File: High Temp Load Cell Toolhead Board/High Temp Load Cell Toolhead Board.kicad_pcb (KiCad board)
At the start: 6 copper layers, 60 x 60 mm, 123 parts, among them J1 Conn_01x03, J11 Conn_01x03, J12 Conn_01x03, J13 PinHeader_2x4_P2.54mm, J2 Conn_02x08, J6 Conn_01x04, J7 Conn_01x02, J8 Conn_01x04, J9 Conn_01x02, P1 USB_C_Plug_USB2.0, Q1 CSD17581Q3A, Q2 CSD17581Q3A, SW1 SW_SPST, U1 SN74LVC2G17DSFR, U2 STM32F103CBU6TR, U3 SN74LVC2G17DSFR, U5 ADS1220, Y1 Crystal

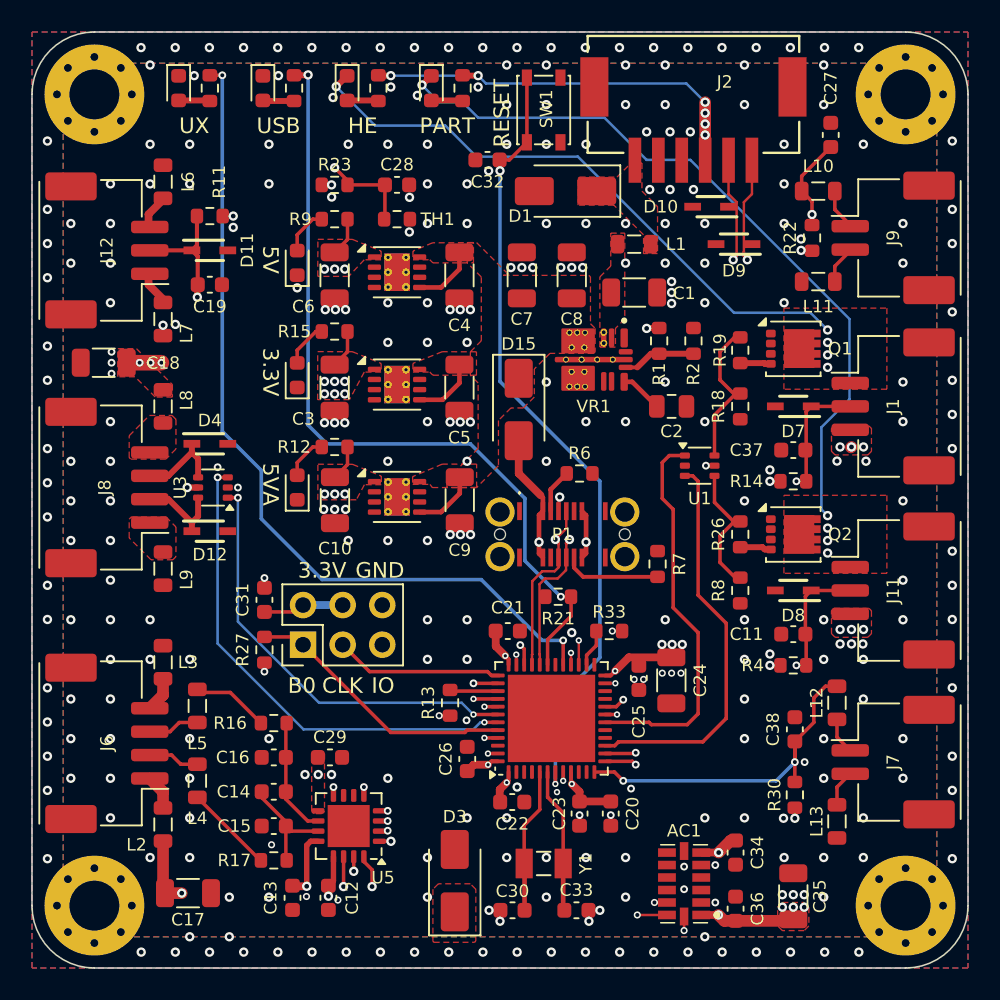
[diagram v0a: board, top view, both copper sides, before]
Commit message: Update 5V Power input
* Changed 5V USB power to rout in via the main 24V power input. This assumes the buck converter can operate in dropout mode and pass the 5V supply to the LDOs. This avoids potential issues with backfeeding the buck converter.
* Added a klipper pins file to give meaningful names to pins
* Added do-not-populate bypass resistors for fans to test tachometer behavior
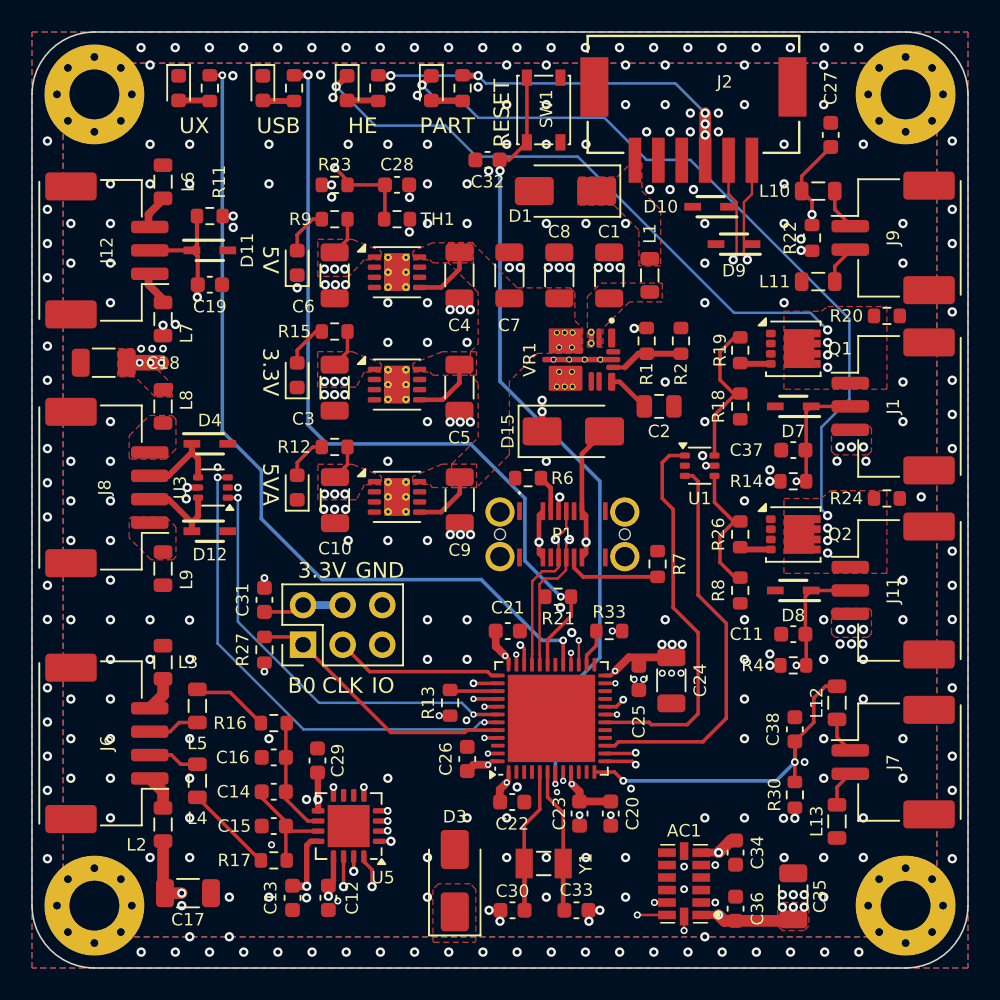
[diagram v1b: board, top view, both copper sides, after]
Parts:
- added R20: R20kΩ, Resistor_SMD:R_0603_1608Metric, F.Cu at (54.8, 18.2)
- added R24: R20kΩ, Resistor_SMD:R_0603_1608Metric, F.Cu at (54.8, 29.9)
- moved D15 3.77 mm to (34.7, 25.6), turned to 0 degrees
- moved R6 3.31 mm to (31.8, 28.6), turned to 180 degrees
- moved L1 2.24 mm to (39.6, 15.6), turned to -90 degrees
- moved C1 1.94 mm to (37.0, 15.6), turned to 90 degrees
- moved C29 0.82 mm to (18.3, 46.7), turned to 90 degrees
- moved C8 0.80 mm to (33.8, 15.6)
- moved R1 0.80 mm to (39.4, 19.8)
- moved C2 0.80 mm to (40.2, 24.0)
- moved C7 0.80 mm to (30.6, 15.6)
- moved R2 0.80 mm to (41.6, 19.8)
- moved VR1 0.80 mm to (35.2, 21.0)
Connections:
- D15 pad 1: +5V5 -> +24V
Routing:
- net +24V: track 0.00 -> 9.56 mm, vias 0 -> 1
- net +5VA: track 58.8 -> 62.8 mm
- net /+FANV_INPUT: track 70.1 -> 69.3 mm, vias 12 -> 11
- net /+5V_USB: track 15.8 -> 16.4 mm
- net +3V3: vias 27 -> 24

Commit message: Add Thermal Reliefs
* Enable thermal relief on GND and 3.3V
* Re-work 5.5V zone to support thermal relief
* Move vias off of silkscreen
* Fix vias that are close to pads
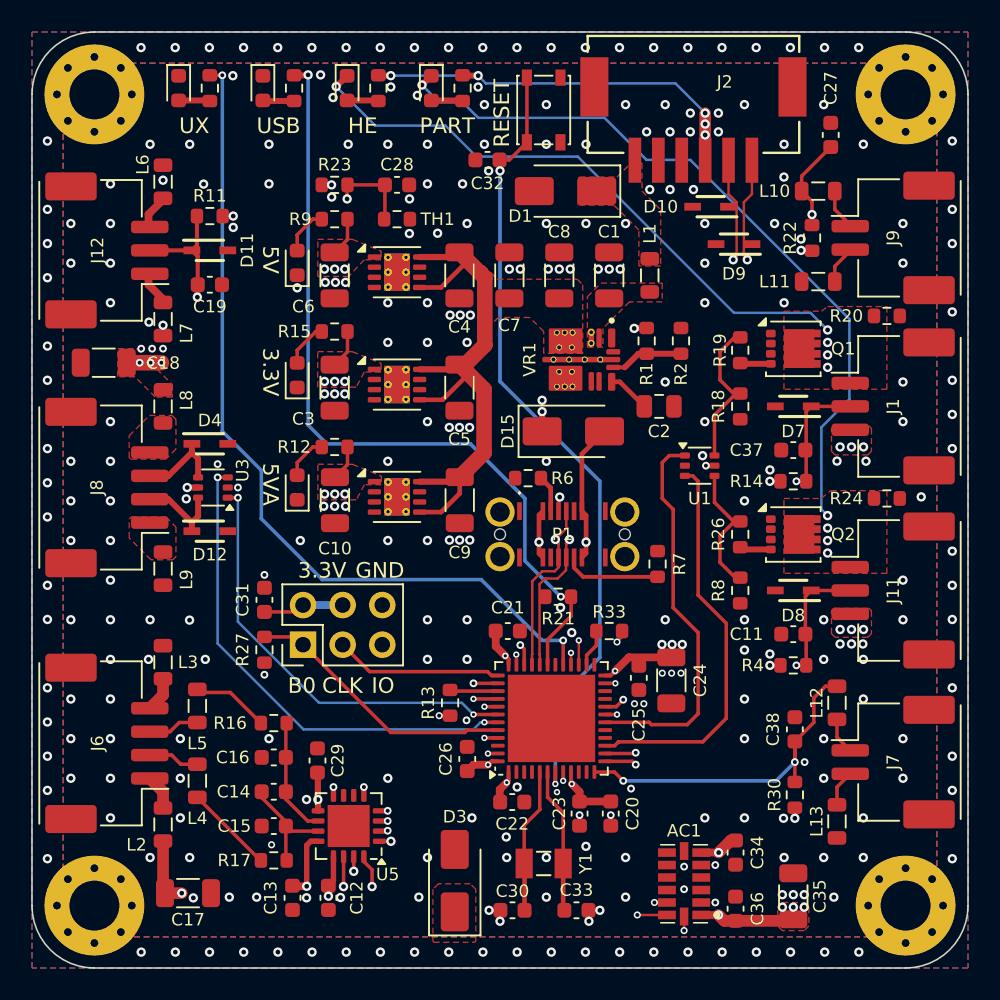
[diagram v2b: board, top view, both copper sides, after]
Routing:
- net +5V5: track 17.8 -> 43.4 mm
- net AMBIENT_THERMISTOR: track 62.0 -> 60.0 mm
- net GND: vias 241 -> 231

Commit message: Add Dotstar Indicator
This change replaces the indicator LED with a Dotstar RGB LED. This allows various conditions to be indicated at the toolhead via colors, brightness and blinking.

* Fixed missing guard ring on layers 4 and 5.
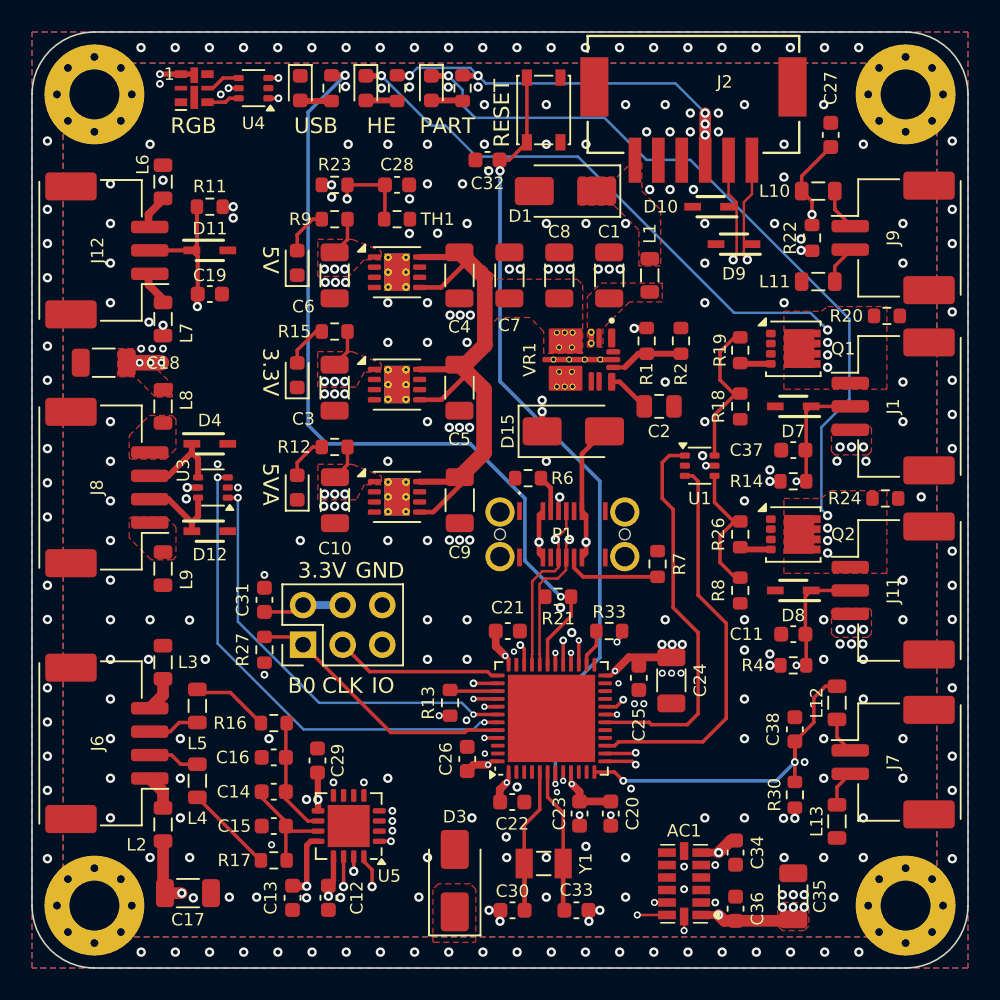
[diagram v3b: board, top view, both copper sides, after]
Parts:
- removed R29: R1kΩ, Resistor_SMD:R_0603_1608Metric
- added U4: SN74LVC2G17DSFR, Package_TO_SOT_SMD:SOT-363_SC-70-6, F.Cu at (14.2, 3.60)
- D16: value RED LED -> DotStar Micro LED; footprint LED_SMD:LED_0603_1608Metric -> LED_SMD:LED-APA102-2020
- moved D6 2.40 mm to (17.2, 3.60)
- moved R10 2.40 mm to (19.2, 3.60)
- moved D13 1.20 mm to (21.4, 3.60)
- moved R3 1.20 mm to (23.4, 3.60)
- moved D16 1.00 mm to (10.4, 3.60), turned to 0 degrees
- moved C19 0.60 mm to (11.4, 16.8)
- moved R11 0.60 mm to (11.4, 11.2)
- moved R24 0.10 mm to (54.7, 29.9)
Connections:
- D16 pad 1: GND -> +5V
- D16 pad 2: Net-(D16-A) -> unconnected-(D16-CKO-Pad2)
- U2 pad 29: INDICATOR_LED -> INDICATOR_LED_CLK
- U2 pad 30: unconnected-(U2-PA9-Pad30) -> INDICATOR_LED_SDO
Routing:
- net INDICATOR_LED_SDO: track 0.00 -> 54.5 mm, vias 0 -> 2
- net INDICATOR_LED: track 54.4 -> 0.00 mm, vias 2 -> 0
- net INDICATOR_LED_CLK: track 0.00 -> 52.3 mm, vias 0 -> 2
- net +5V: track 63.7 -> 84.6 mm, vias 8 -> 10
- net AMBIENT_THERMISTOR: track 60.0 -> 52.8 mm
- net /FAN0_MOSFET_GND: track 38.9 -> 36.4 mm
- net /RGB_INDICATOR_CLK: track 0.00 -> 2.27 mm
- net /RGB_INDICATOR_SDO: track 0.00 -> 2.10 mm
- net Net-(D16-A): track 2.02 -> 0.00 mm
- net USB_PULL_UP: track 52.1 -> 53.0 mm
- net /+FANV_INPUT: track 69.3 -> 68.5 mm
- net /FAN1_MOSFET_GND: track 48.0 -> 47.4 mm
- net FILAMENT_SW: track 50.5 -> 51.1 mm
- net GND: vias 231 -> 218
- added copper zone on In3.Cu, net Earth_Protective
- added copper zone on In4.Cu, net Earth_Protective
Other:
- board text added: "RGB"
- board text removed: "UX"
